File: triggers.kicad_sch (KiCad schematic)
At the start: 27 parts, among them U1202 74HC2G17, U1207 74HC2G17, U1208 74HC2G17

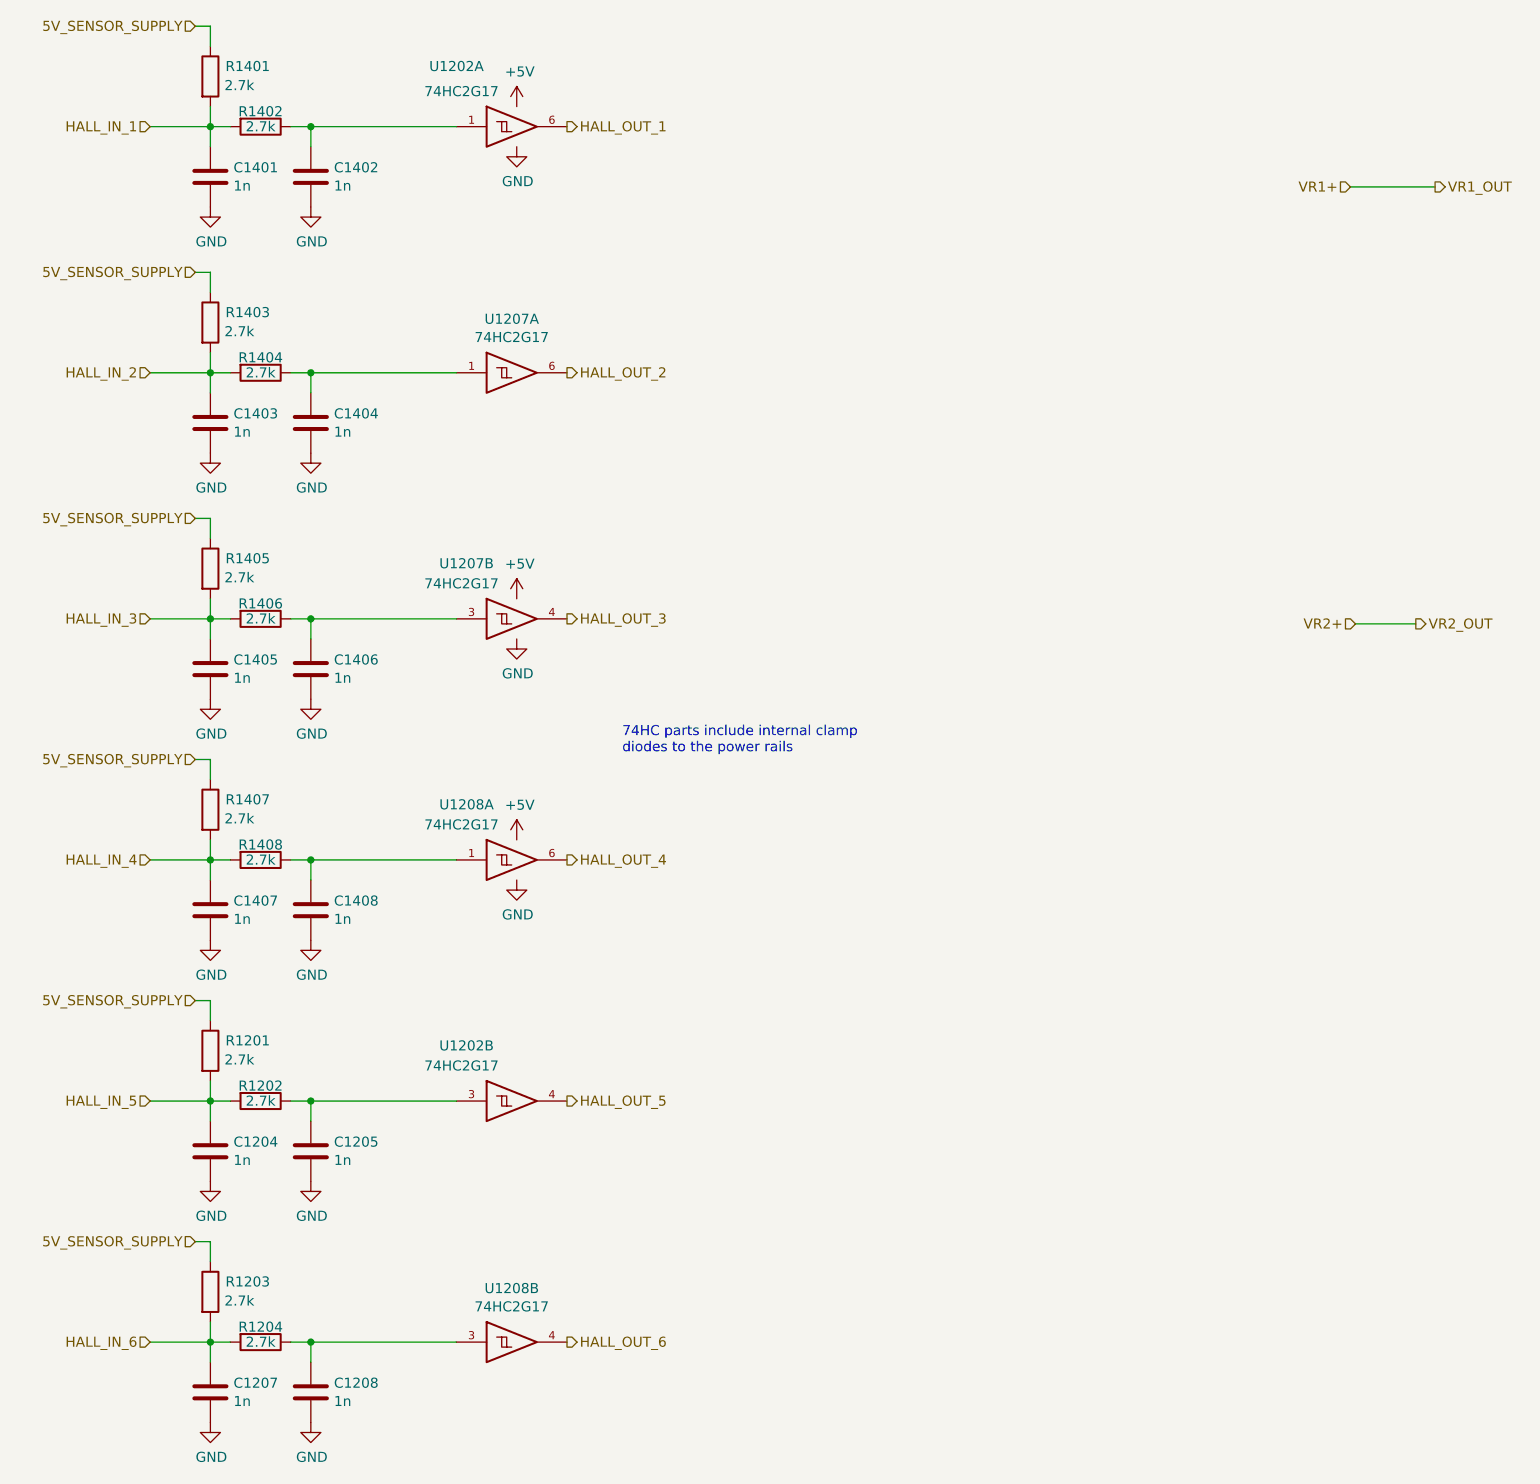
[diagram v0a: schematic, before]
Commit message: Right hand pinout completed
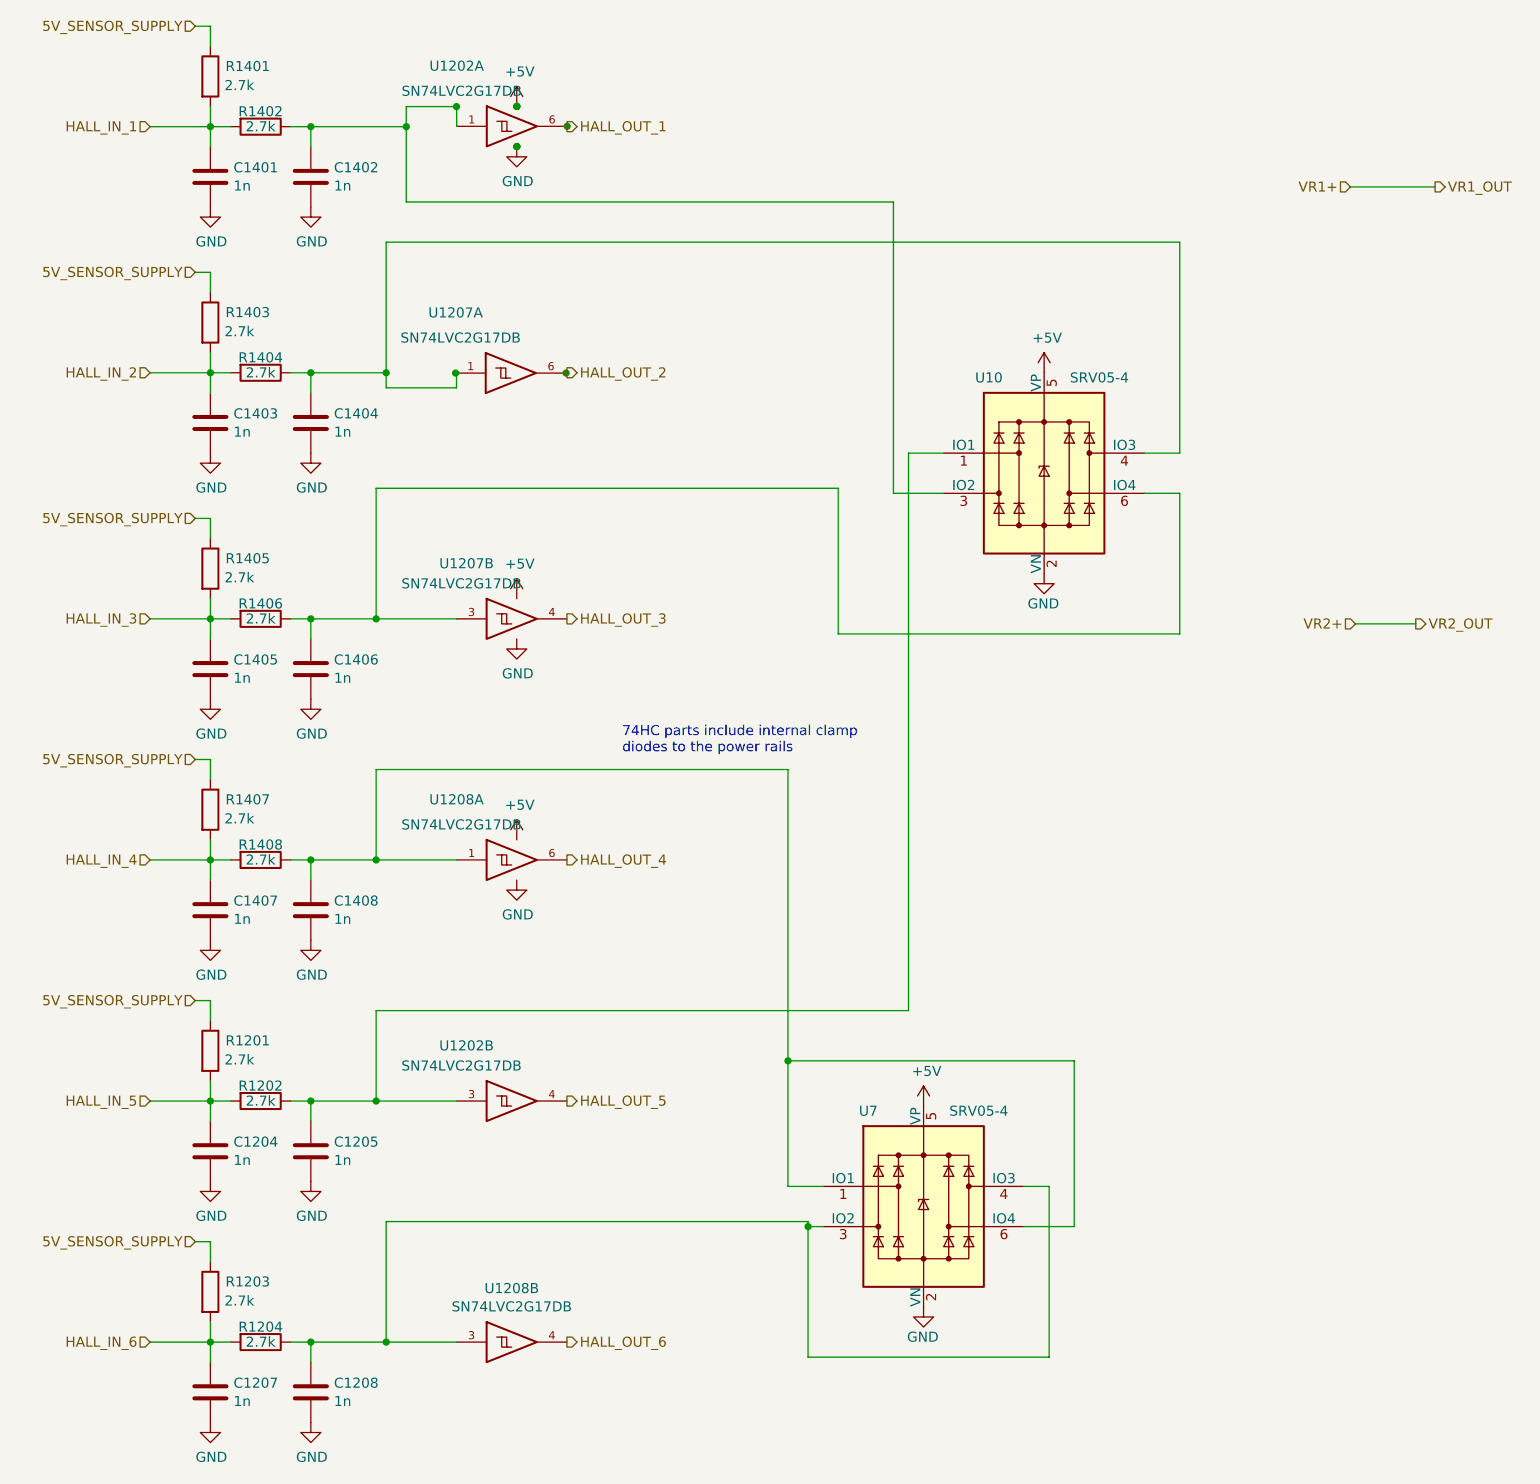
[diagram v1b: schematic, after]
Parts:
- added U10, U7: SRV05-4, Package_TO_SOT_SMD:SOT-23-6, symbol Power_Protection:SRV05-4
- U1202, U1207, U1208: value 74HC2G17 -> SN74LVC2G17DB; footprint Package_TO_SOT_SMD:SOT-363_SC-70-6 -> Package_TO_SOT_SMD:SOT-23-6; LCSC C94189 -> C10429
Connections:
- net +5V: now also U10.5 (VP), U7.5 (VP)
- net GND: now also U10.2 (VN), U7.2 (VN)
- net at C1205.1, R1202.1, U1202.3: now also U10.1 (IO1)
- net at C1208.1, R1204.1, U1208.3: now also U7.3 (IO2), U7.4 (IO3)
- net at C1402.1, R1402.1, U1202.1: now also U10.3 (IO2)
- net at C1404.1, R1404.1, U1207.1: now also U10.4 (IO3)
- net at C1406.1, R1406.1, U1207.3: now also U10.6 (IO4)
- net at C1408.1, R1408.1, U1208.1: now also U7.1 (IO1), U7.6 (IO4)
